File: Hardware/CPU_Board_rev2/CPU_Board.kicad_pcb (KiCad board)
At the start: 2 copper layers, 100 x 70 mm, 100 parts, among them P1 CONN_01X02, P10 CONN_01X02, P11 CONN_01X06, P12 CONN_01X03, P13 CONN_01X01, P14 CONN_01X03, P15 CONN_01X01, P16 CONN_01X01, P17 CONN_01X01, P18 CONN_01X03, P19 CONN_01X01, P2 USB_B, P20 CONN_01X01, P21 CONN_01X06, P22 CONN_01X01, P23 CONN_01X01, P24 CONN_01X06, P25 CONN_01X04, P26 CONN_01X04, P3 CONN_01X04, P4 CONN_01X04, P5 CONN_01X06, P7 CONN_01X02, P8 CONN_01X02, P9 CONN_01X02, Q1 Q_PMOS_GSD, Q2 Q_PNP_BCE, Q3 Q_PNP_BCE, U1 STM32F411RETx, U10 MCDTS2-4N, U11 LPS22HB, U12 INA128, U2 NCP1117DT12G, U3 FT232RL, U4 HTS221, U5 INA128, U6 SPBTLE-RF, U7 A2235-H, U8 LSM303AGR, U9 LSM6DSL, Y1 8MHz

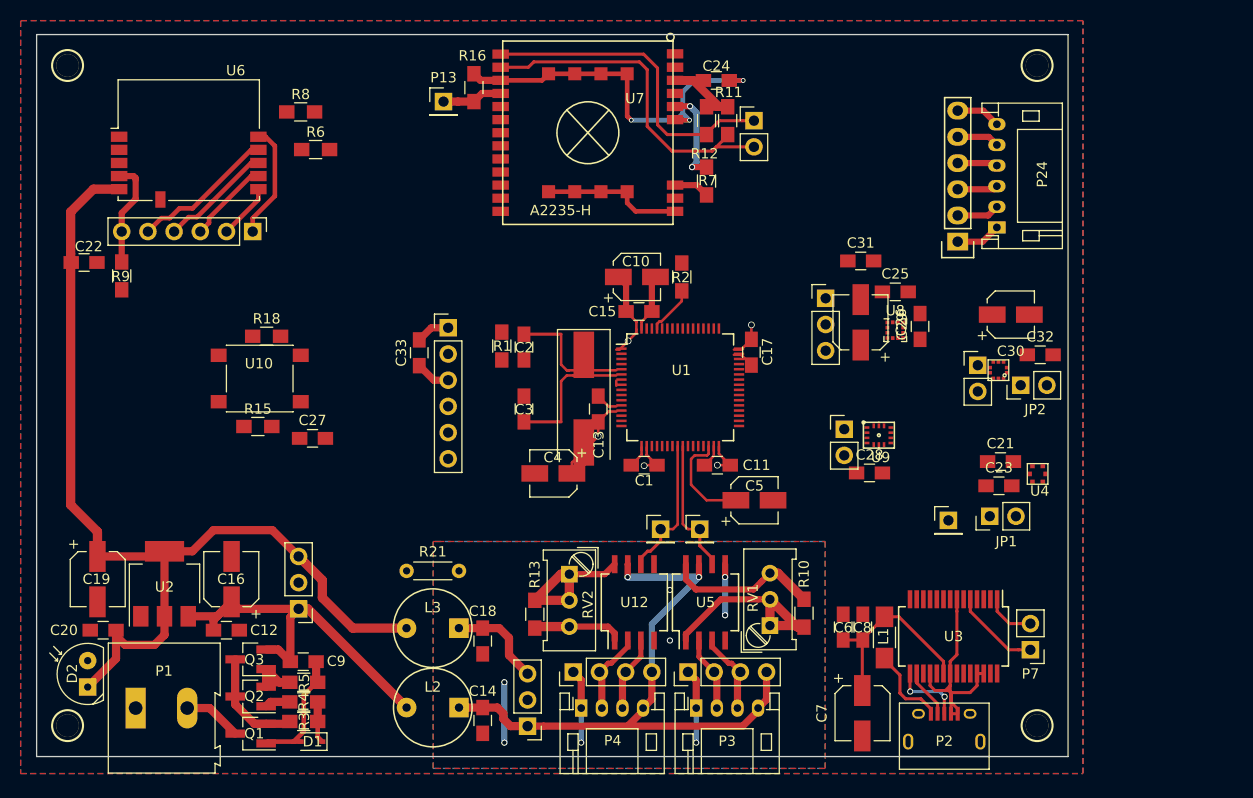
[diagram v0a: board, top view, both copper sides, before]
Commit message: Chackpoint PCB rev2
* Added datasheets for LSM9DS1 and STEVAL board
* Drawn footprints for:
o Connectors (JST)
o LGA-12_2x2mm "Handsolder friendlier"
o LGA-24L_3x3.5 "Handsolder friendlier"
* Drawn symbol for LSM9DS1
* Fixed GPS A2235-H footprints (normal & Handsolder)
* Almost completed MCU-board rev2 schematic (Miss connections for
LSM9DS1)
* Almost completed MCU-board rev2 PCB layout (Miss the connections for
LSM and have only designed internal module layout for all IMU/IMU-like
components.)

Next steps:
* Make space for gigantig STEVAL LSM9DS1 DIP24
* Draw connections to MCU
* Cake
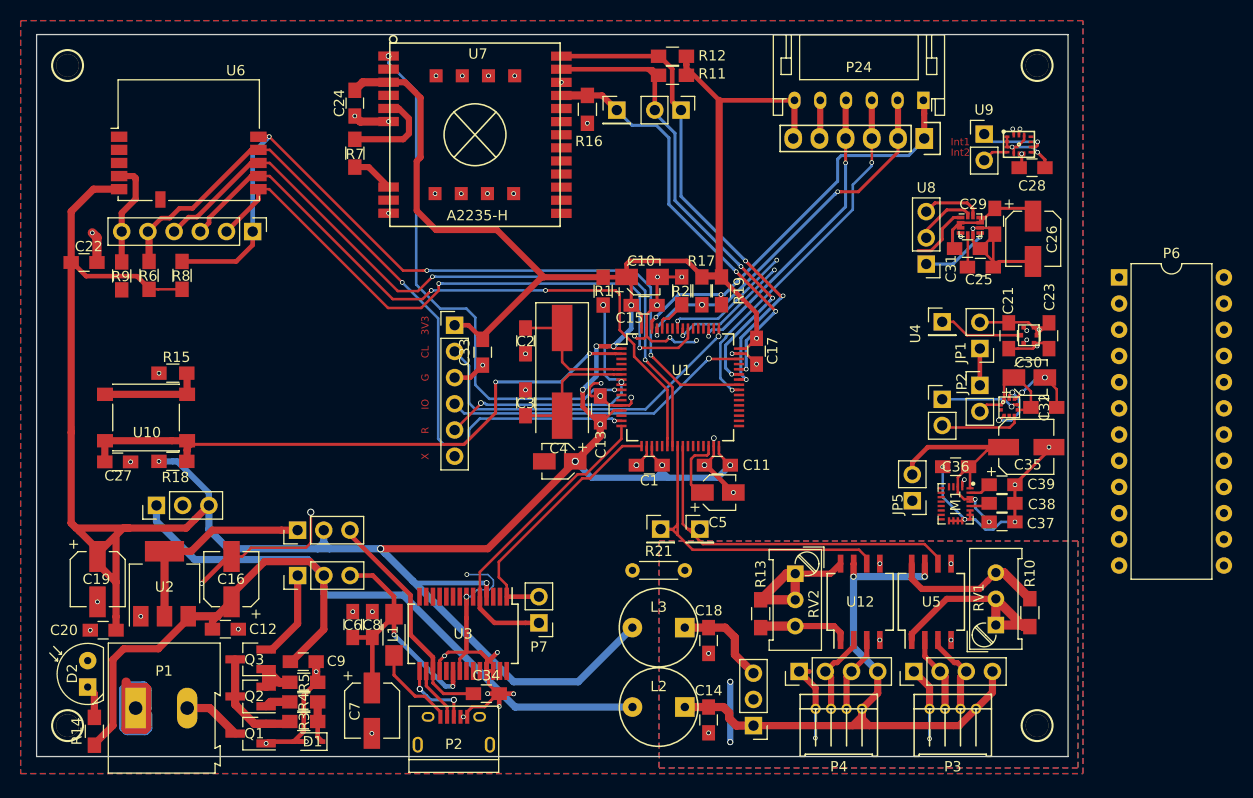
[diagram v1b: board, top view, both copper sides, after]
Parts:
- added C34: 100n, Capacitors_SMD:C_0805_HandSoldering, F.Cu at (87.2, 166.2)
- added C35: 10uF, Capacitors_SMD:CP_Elec_5x5.3, F.Cu at (139.5, 142.3)
- added C36: 100n, Capacitors_SMD:C_0805_HandSoldering, F.Cu at (132.7, 144.2)
- added C37: 100n, Capacitors_SMD:C_0805_HandSoldering, F.Cu at (137.2, 149.6)
- added C38: 10n, Capacitors_SMD:C_0805_HandSoldering, F.Cu at (137.2, 147.8)
- added C39: 100n, Capacitors_SMD:C_0805_HandSoldering, F.Cu at (137.2, 146.0)
- added IM1: LSM9DS1, FOOTPRINTS:LGA-24L_3x3.5mm_Pitch0.43mm_Handsolder, F.Cu at (132.7, 147.8)
- added JP3: Jumper_NC_Dual, Pin_Headers:Pin_Header_Straight_1x03_Pitch2.54mm, F.Cu at (68.9, 154.8)
- added JP4: Jumper_NC_Dual, Pin_Headers:Pin_Header_Straight_1x03_Pitch2.54mm, F.Cu at (68.8, 150.4)
- added JP5: Jumper_NC_Small, Pin_Headers:Pin_Header_Straight_1x02_Pitch2.54mm, F.Cu at (128.4, 147.6)
- added P6: CONN_02X12, Housings_DIP:DIP-24_W10.16mm, F.Cu at (148.5, 125.9)
- added R14: 220, Resistors_SMD:R_0805_HandSoldering, F.Cu at (49.1, 169.9)
- added R17: 10k, Resistors_SMD:R_0805_HandSoldering, F.Cu at (108.0, 127.2)
- added R19: 10k, Resistors_SMD:R_0805_HandSoldering, F.Cu at (110.0, 127.2)
- C10, C30, C4, C5: footprint Capacitors_SMD:CP_Elec_4x5.3 -> Capacitors_SMD:CP_Elec_3x5.3
- P24: footprint Connectors_JST:JST_PH_S6B-PH-K_06x2.00mm_Angled -> FOOTPRINTS:JST_PH_S6B-PH-K_06x2.50mm_Angled
- P3, P4: footprint Connectors_JST:JST_PH_S4B-PH-K_04x2.00mm_Angled -> FOOTPRINTS:Connector_JST_S4B-ZR_1x4
- U8: footprint Housings_LGA:LGA-12_2x2mm_Pitch0.5mm -> FOOTPRINTS:LGA-12_2x2mm_Pitch0.5mm_Handsolder
- moved P7 47.7 mm to (92.2, 159.4)
- moved P2 47.6 mm to (84.0, 169.8)
- moved C8 47.6 mm to (76.1, 159.6)
- moved C6 47.6 mm to (74.2, 159.6)
- moved C7 47.6 mm to (76.0, 167.9)
- moved L1 47.6 mm to (78.2, 160.6)
- moved U3 47.6 mm to (84.9, 160.4)
- moved C24 35.1 mm to (74.4, 109.0), turned to 270 degrees
- moved R7 34.2 mm to (74.4, 113.8)
- moved C28 33.5 mm to (140.1, 115.3), turned to 180 degrees
- moved P9 31.7 mm to (135.4, 112.0)
- moved U9 31.3 mm to (137.6, 112.3)
- moved P4 25.0 mm to (121.3, 169.5)
- moved P3 24.9 mm to (132.4, 169.5)
- moved C14 21.9 mm to (108.7, 168.8)
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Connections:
- net /BT_10_PA1 renamed /BT_CL
- net /BT_11_PA8 renamed /BT_RST
- net /BT_4_PA0 renamed /BT_IRQ
- net /BT_7_PB3 renamed /BT_CS
- net /BT_8_PA6 renamed /BT_MISO
- net /BT_9_PA7 renamed /BT_MOSI
- net Net-(C6-Pad1) renamed /USB5V
- D2 pad 1: +3V3 -> Net-(D2-Pad1)
- Q3 pad 2: +5V -> Net-(JP3-Pad1)
- U2 pad 2: +3V3 -> Net-(JP4-Pad1)
- U2 pad 4: +3V3 -> Net-(JP4-Pad1)
- U3 pad 17: (no net) -> /USB3V3
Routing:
- net +3V3: track 142.3 -> 363.5 mm, vias 5 -> 14
- net GND: track 108.9 -> 196.5 mm, vias 3 -> 64
- net /BT_RST: track 11.2 -> 79.1 mm, vias 0 -> 3
- net +5V: track 37.8 -> 101.9 mm
- net /BT_MOSI: track 10.9 -> 70.9 mm, vias 0 -> 2
- net /U_BUT: track 0.00 -> 59.8 mm, vias 0 -> 2
- net /BT_CL: track 14.1 -> 72.6 mm, vias 0 -> 2
- net /BT_MISO: track 8.13 -> 65.2 mm, vias 0 -> 2
- net /BT_CS: track 5.39 -> 60.2 mm, vias 0 -> 2
- net /GPS_NRST: track 0.00 -> 51.9 mm, vias 0 -> 2
- net /IMU_I2C_DA: track 4.37 -> 41.9 mm, vias 0 -> 5
- net /IMU_I2C_CL: track 8.01 -> 44.0 mm, vias 0 -> 6
- net /GPS_TOGGLE: track 5.87 -> 40.7 mm, vias 0 -> 3
- net /SWCLK: track 0.00 -> 33.7 mm, vias 0 -> 1
- net /VL_C9: track 3.92 -> 35.1 mm, vias 0 -> 2
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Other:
- board text added: "3V3"
- board text added: "CL"
- board text added: "G"
- board text added: "IO"
- board text added: "Int1"
- board text added: "Int2"
- board text added: "R"
- board text added: "X"

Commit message: PCB rev2.0 complete-ish
Rev 2 completed, except for LSM9DS1 ports: "SDO-A/G", "SDO-M" and "Data
enable A/G"
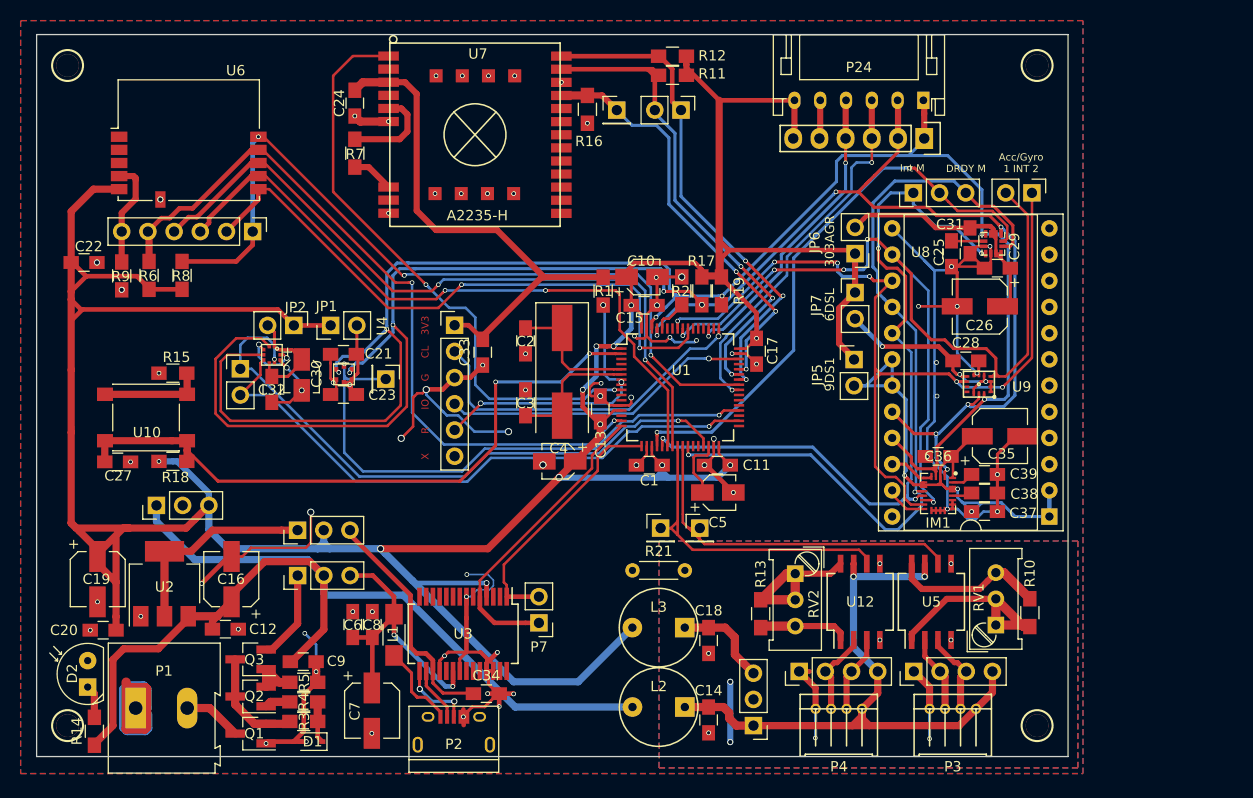
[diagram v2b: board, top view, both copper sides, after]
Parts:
- added JP6: Jumper_NC_Small, Pin_Headers:Pin_Header_Straight_1x02_Pitch2.54mm, F.Cu at (122.9, 123.6)
- added JP7: Jumper_NC_Small, Pin_Headers:Pin_Header_Straight_1x02_Pitch2.54mm, F.Cu at (122.9, 127.4)
- P6: footprint Housings_DIP:DIP-24_W10.16mm -> Housings_DIP:DIP-24_W15.24mm_Socket
- moved C32 74.9 mm to (66.3, 136.8), turned to 270 degrees
- moved U11 71.7 mm to (66.4, 133.4), turned to 90 degrees
- moved C30 70.6 mm to (69.2, 135.3), turned to 270 degrees
- moved C23 68.6 mm to (73.3, 137.2), turned to 180 degrees
- moved P10 68.1 mm to (63.3, 134.8)
- moved JP2 66.8 mm to (68.5, 130.6), turned to 270 degrees
- moved U4 66.5 mm to (73.3, 135.3), turned to 270 degrees
- moved C21 64.5 mm to (73.3, 133.3), turned to 180 degrees
- moved JP1 63.0 mm to (72.1, 130.6), turned to 90 degrees
- moved P15 54.2 mm to (77.4, 135.8), turned to 270 degrees
- moved U9 24.8 mm to (136.1, 137.0), turned to 180 degrees
- moved P6 24.2 mm to (141.7, 149.1), turned to 180 degrees
- moved C28 19.8 mm to (133.6, 134.0), turned to 0 degrees
- moved JP5 14.8 mm to (122.8, 133.9), turned to 0 degrees
- moved C26 8.33 mm to (135.0, 128.7), turned to 180 degrees
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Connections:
- C26 pad 1: +3V3 -> /LSM303_VDD
- C28 pad 1: +3V3 -> /LSM6_VDD
- C29 pad 1: +3V3 -> /LSM303_VDD
- C31 pad 1: +3V3 -> /LSM303_VDD
- C35 pad 1: /LSM9_VDD -> /LSM9_CS_A/G
- C36 pad 1: /LSM9_VDD -> /LSM9_CS_A/G
- C37 pad 1: /LSM9_VDD -> /LSM9_CS_A/G
- IM1 pad 1: /LSM9_VDD -> /LSM9_CS_A/G
- IM1 pad 10: /LSM9_INT_M -> /INT_Mag
- IM1 pad 11: /LSM9_INT1_A/G -> /LSM6DSL_INT1
- IM1 pad 12: /LSM9_INT2_A/G -> /LSM6DSL_INT2
- IM1 pad 22: /LSM9_VDD -> /LSM9_CS_A/G
- IM1 pad 23: /LSM9_VDD -> /LSM9_CS_A/G
- IM1 pad 3: /LSM9_VDD -> /LSM9_CS_A/G
- IM1 pad 4: /LSM9_SDA -> /IMU_I2C_DA
- IM1 pad 8: /LSM9_CS_M -> /LSM9_CS_A/G
- IM1 pad 9: /LSM9_DRDY_M -> /DRDY_Mag
- JP5 pad 2: /LSM9_VDD -> /LSM9_CS_A/G
- P14 pad 1: /303C_I_MAG -> /INT_Mag
- P14 pad 3: /303C_DRDY -> /DRDY_Mag
- P6 pad 1: /LSM9_VDD -> /LSM9_CS_A/G
- P6 pad 14: /LSM9_INT1_A/G -> /LSM6DSL_INT1
- P6 pad 15: /LSM9_INT2_A/G -> /LSM6DSL_INT2
- P6 pad 16: /LSM9_DRDY_M -> /DRDY_Mag
- P6 pad 17: /LSM9_INT_M -> /INT_Mag
- P6 pad 18: /LSM9_CS_M -> /LSM9_CS_A/G
- P6 pad 2: /LSM9_VDD -> /LSM9_CS_A/G
- P6 pad 21: /LSM9_SDA -> /IMU_I2C_DA
- U1 pad 21: /303C_I_MAG -> /INT_Mag
- U1 pad 26: /303C_DRDY -> /DRDY_Mag
- U8 pad 10: +3V3 -> /LSM303_VDD
- U8 pad 11: /303C_DRDY -> /DRDY_Mag
- U8 pad 2: +3V3 -> /LSM303_VDD
- U8 pad 3: +3V3 -> /LSM303_VDD
- U8 pad 7: /303C_I_MAG -> /INT_Mag
- U8 pad 9: +3V3 -> /LSM303_VDD
- U9 pad 1: +3V3 -> /LSM6_VDD
- U9 pad 12: +3V3 -> /LSM6_VDD
- U9 pad 2: +3V3 -> /LSM6_VDD
- U9 pad 3: +3V3 -> /LSM6_VDD
- U9 pad 5: +3V3 -> /LSM6_VDD
- U9 pad 8: +3V3 -> /LSM6_VDD
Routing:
- net /IMU_I2C_CL: track 44.0 -> 175.7 mm, vias 6 -> 10
- net /IMU_I2C_DA: track 41.9 -> 170.0 mm, vias 5 -> 6
- net /LSM6DSL_INT1: track 14.7 -> 94.7 mm, vias 2 -> 5
- net /DRDY_Mag: track 0.00 -> 78.9 mm, vias 0 -> 2
- net /INT_Mag: track 0.00 -> 75.4 mm, vias 0 -> 4
- net /LSM6DSL_INT2: track 19.3 -> 85.7 mm, vias 3 -> 6
- net GND: track 196.5 -> 257.7 mm, vias 64 -> 75
- net /LSM9_CS_A/G: track 0.00 -> 53.3 mm, vias 0 -> 3
- net /LPS_DRDY: track 7.68 -> 60.9 mm, vias 1 -> 2
- net /LPS_SA0: track 7.97 -> 58.6 mm, vias 0 -> 1
- net /303C_I_XL: track 5.91 -> 56.1 mm, vias 0 -> 2
- net /HTS_DRDY: track 8.19 -> 54.5 mm, vias 0 -> 2
- net +3V3: track 363.5 -> 396.8 mm, vias 14 -> 12
- net /LSM9_VDD: track 25.6 -> 0.00 mm, vias 2 -> 0
- net /LSM303_VDD: track 0.00 -> 25.3 mm
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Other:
- board text added: "303AGR"
- board text added: "6DSL"
- board text added: "9DS1"
- board text added: "Acc/Gyro 1 INT 2"
- board text added: "DRDY M"
- board text added: "Int M"
- board text removed: "Int1"
- board text removed: "Int2"

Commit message: Silkscreen annotations
Good-ish looking silkscreen~~
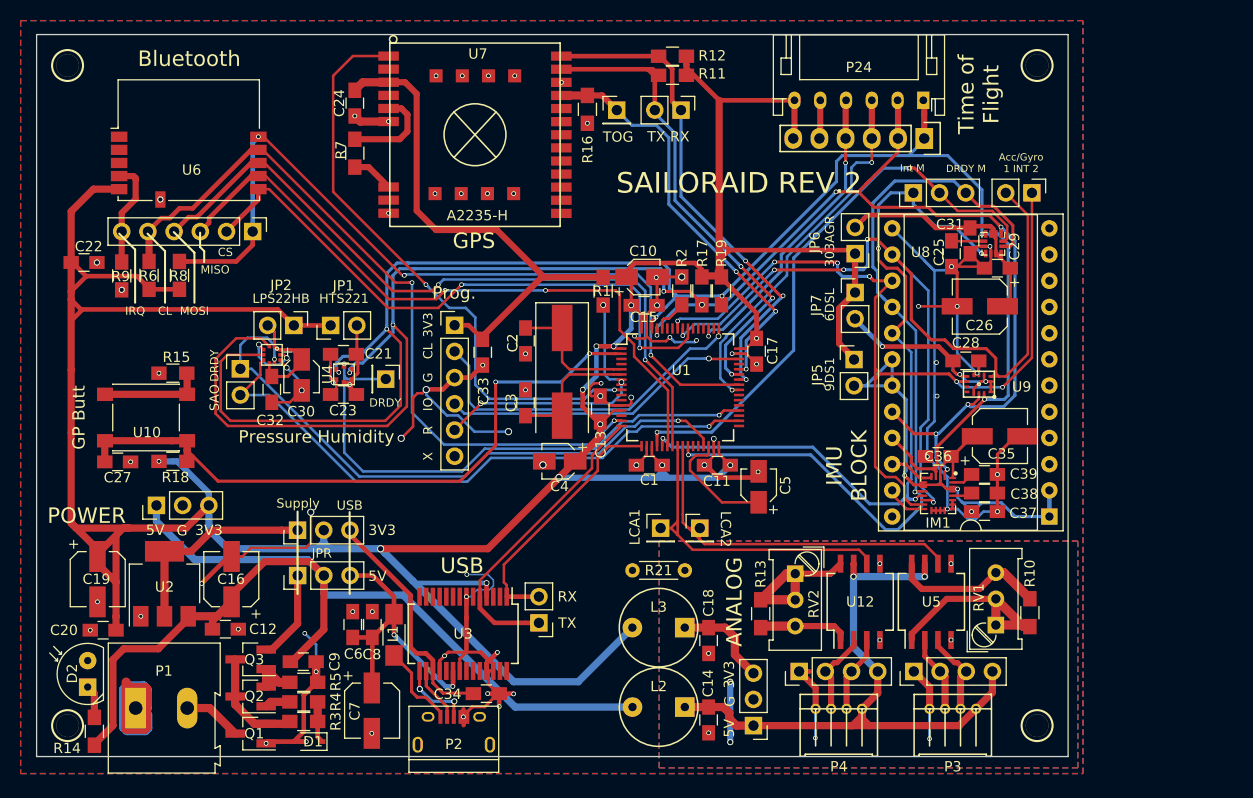
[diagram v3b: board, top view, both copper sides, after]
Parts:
- moved C5 3.99 mm to (113.5, 146.2), turned to 90 degrees
- moved R8 0.25 mm to (57.4, 125.7)
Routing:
- net Net-(C5-Pad1): track 6.10 -> 11.7 mm
- net GND: track 257.7 -> 259.8 mm
- net /BT_RST: track 78.7 -> 79.4 mm
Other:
- board text added: "5V"
- board text added: "ANALOG"
- board text added: "Bluetooth"
- board text added: "CS"
- board text added: "DRDY"
- board text added: "GP Butt"
- board text added: "GPS"
- board text added: "HTS221"
- board text added: "IMU BLOCK"
- board text added: "IRQ"
- board text added: "JPR"
- board text added: "LCA1"
- board text added: "LCA2"
- board text added: "LPS22HB"
- board text added: "MISO"
- board text added: "MOSI"
- board text added: "POWER"
- board text added: "Pressure Humidity"
- board text added: "Prog."
- board text added: "RX"
- board text added: "SAILORAID REV.2"
- board text added: "SAO"
- board text added: "Supply"
- board text added: "TOG"
- board text added: "TX"
- board text added: "TX RX"
- board text added: "Time of Flight"
- board text added: "USB"

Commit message: PCB rev2 complete
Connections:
- IM1 pad 5: /LSM9_SDO -> GND
- IM1 pad 6: /LSM9_SDO -> GND
- P6 pad 22: /LSM9_SDO -> GND
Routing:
- net GND: track 259.8 -> 264.7 mm, vias 75 -> 76
- net /LSM9_SDO: track 4.42 -> 0.00 mm

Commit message: Complete PCB rev2.1
Completed, rendered gerbers, rendered drill and order sent to Jan
refering to myself as his dear friend.
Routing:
- net GND: track 264.7 -> 451.5 mm, vias 76 -> 116

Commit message: Stuff for rev 3...
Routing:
- net GND: track 451.5 -> 459.6 mm
- net /IMU_I2C_CL: track 175.7 -> 174.8 mm
- net /HTS_VDD: track 10.6 -> 11.5 mm, vias 1 -> 0
- net /LSM6_VDD: track 20.7 -> 21.5 mm
- net /HTS_DRDY: track 54.5 -> 54.0 mm

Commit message: Fixes
Some fixes (now implemented to the PCB)
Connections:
- P11 pad 2: /BT_CS -> /BT_CLK
- P11 pad 5: /BT_CL -> /BT_CS
- R6 pad 1: /BT_CL -> /BT_CS
- U1 pad 14: (no net) -> /BT_IRQ
- U1 pad 15: /BT_CL -> /BT_CS
- U1 pad 55: /BT_CS -> /BT_CLK
- U6 pad 10: /BT_CL -> /BT_CS
- U6 pad 7: /BT_CS -> /BT_CLK
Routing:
- net /BT_CL: track 72.4 -> 0.00 mm, vias 2 -> 0
- net /BT_IRQ: track 12.4 -> 73.3 mm, vias 0 -> 2
- net /BT_CLK: track 0.00 -> 60.3 mm, vias 0 -> 2
- net (no net): track 5.85 -> 24.1 mm, vias 2 -> 11
- net GND: track 459.6 -> 444.2 mm, vias 116 -> 107
- net /BT_CS: track 59.7 -> 72.4 mm
- net /BT_RST: track 79.4 -> 78.3 mm

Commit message: Rev 2 last ed. Rev 3 "merge"
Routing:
- net /LSM6DSL_INT1: track 95.1 -> 92.5 mm
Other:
- board text added: "C10"
- board text added: "DA"
- board text added: "SD"
